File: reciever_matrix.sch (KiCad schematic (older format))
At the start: 1 part, among them J2 QUARTET_RECV

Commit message: Layout and route numpad matrix
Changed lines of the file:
@@
 $Descr A4 11693 8268
 encoding utf-8
-Sheet 3 3
+Sheet 3 4
 Title ""
 Date ""
@@
 AR Path="/5FF53271/5FF867A2" Ref="#PWR?"  Part="1"
 AR Path="/5FF53271/5FF7CBCC/5FF867A2" Ref="#PWR?"  Part="1"
-AR Path="/5FF5604D/5FF9299E/5FF867A2" Ref="#PWR?"  Part="1"
+AR Path="/5FF5604D/5FF9299E/5FF867A2" Ref="#PWR01"  Part="1"
 AR Path="/5FF77C9D/5FF867A2" Ref="#PWR03"  Part="1"
-F 0 "#PWR03" H 1350 950 50  0001 C CNN
+F 0 "#PWR01" H 1350 950 50  0001 C CNN
 F 1 "+5V" H 1365 1273 50  0000 C CNN
 F 2 "" H 1350 1100 50  0001 C CNN
@@
 AR Path="/5FF53271/5FF867A8" Ref="#PWR?"  Part="1"
 AR Path="/5FF53271/5FF7CBCC/5FF867A8" Ref="#PWR?"  Part="1"
-AR Path="/5FF5604D/5FF9299E/5FF867A8" Ref="#PWR?"  Part="1"
+AR Path="/5FF5604D/5FF9299E/5FF867A8" Ref="#PWR02"  Part="1"
 AR Path="/5FF77C9D/5FF867A8" Ref="#PWR04"  Part="1"
-F 0 "#PWR04" H 1350 1350 50  0001 C CNN
+F 0 "#PWR02" H 1350 1350 50  0001 C CNN
 F 1 "GND" H 1355 1427 50  0000 C CNN
 F 2 "" H 1350 1600 50  0001 C CNN
@@
 	1350 1400 1350 1500
 Connection ~ 1350 1500
-Text GLabel 1350 2250 0    50   Input ~ 0
-PD1
 Text GLabel 1350 2150 0    50   Input ~ 0
 PD0
-Text GLabel 1350 2350 0    50   Input ~ 0
-PD5
-Text GLabel 1350 2450 0    50   Input ~ 0
-PD6
-Text GLabel 1350 2550 0    50   Input ~ 0
-PD7
-Text GLabel 1350 2650 0    50   Input ~ 0
-PB0
-Text GLabel 1350 2750 0    50   Input ~ 0
-PB1
-Text GLabel 1350 2850 0    50   Input ~ 0
-PB2
-Text GLabel 1350 2950 0    50   Input ~ 0
-PC2
-Text GLabel 1350 3050 0    50   Input ~ 0
-PC3
 Text GLabel 1350 3150 0    50   Input ~ 0
 ADC7
-Wire Wire Line
-	1350 3150 1450 3150
-Wire Wire Line
-	1450 3050 1350 3050
-Wire Wire Line
-	1350 2950 1450 2950
-Wire Wire Line
-	1450 2850 1350 2850
-Wire Wire Line
-	1350 2750 1450 2750
-Wire Wire Line
-	1450 2650 1350 2650
-Wire Wire Line
-	1350 2550 1450 2550
-Wire Wire Line
-	1450 2450 1350 2450
-Wire Wire Line
-	1350 2350 1450 2350
-Wire Wire Line
-	1450 2250 1350 2250
-Wire Wire Line
-	1350 2150 1450 2150
 Text GLabel 1350 3350 0    50   Input ~ 0
 MISO
@@
 Text GLabel 1350 3550 0    50   Input ~ 0
 SCL
-Wire Wire Line
-	1350 3250 1450 3250
-Wire Wire Line
-	1350 3350 1450 3350
-Wire Wire Line
-	1350 3450 1450 3450
-Wire Wire Line
-	1350 3550 1450 3550
-Wire Wire Line
-	1350 3650 1450 3650
 $Comp
 L gigahawk:QUARTET_RECV J2
@@
 	1    0    0    -1
 $EndComp
+Text GLabel 1350 2250 0    50   Input ~ 0
+PD1
+Text GLabel 1350 2350 0    50   Input ~ 0
+PD5
+Text GLabel 1350 2450 0    50   Input ~ 0
+PD6
+Text GLabel 1350 2550 0    50   Input ~ 0
+PD7
+Text GLabel 1350 2650 0    50   Input ~ 0
+PB0
+Text GLabel 1350 2750 0    50   Input ~ 0
+PB1
+Text GLabel 1350 2850 0    50   Input ~ 0
+PB2
+Text GLabel 1350 2950 0    50   Input ~ 0
+PC2
+Text GLabel 1350 3050 0    50   Input ~ 0
+PC3
+Wire Wire Line
+	1450 2150 1350 2150
+Wire Wire Line
+	1350 2250 1450 2250
+Wire Wire Line
+	1450 2350 1350 2350
+Wire Wire Line
+	1350 2450 1450 2450
+Wire Wire Line
+	1450 2550 1350 2550
+Wire Wire Line
+	1350 2650 1450 2650
+Wire Wire Line
+	1450 2750 1350 2750
+Wire Wire Line
+	1350 2850 1450 2850
+Wire Wire Line
+	1450 2950 1350 2950
+Wire Wire Line
+	1350 3050 1450 3050
+Wire Wire Line
+	1450 3150 1350 3150
+Wire Wire Line
+	1350 3250 1450 3250
+Wire Wire Line
+	1350 3350 1450 3350
+Wire Wire Line
+	1450 3450 1350 3450
+Wire Wire Line
+	1350 3550 1450 3550
+Wire Wire Line
+	1450 3650 1350 3650
 $EndSCHEMATC

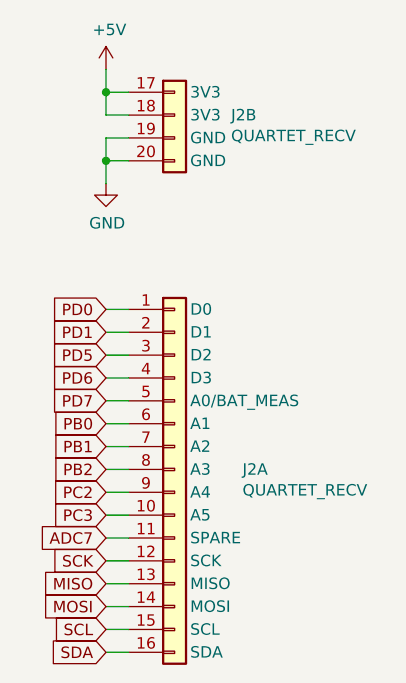
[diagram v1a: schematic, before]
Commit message: Reroute matrix, redo schematics for feather compat
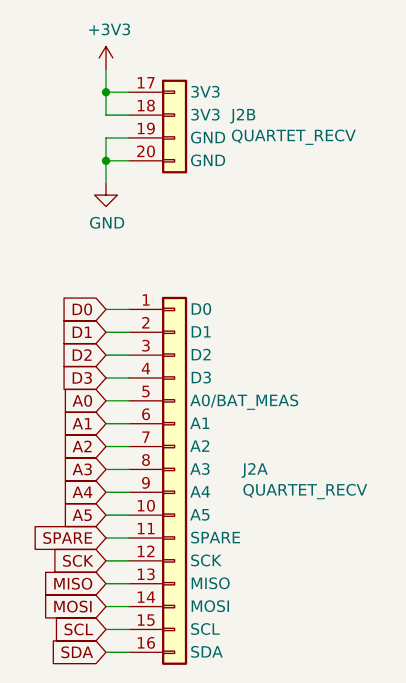
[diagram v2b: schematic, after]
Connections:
- net +5V renamed +3V3
- net ADC7 renamed SPARE
- net PB0 renamed A1
- net PB1 renamed A2
- net PB2 renamed A3
- net PC2 renamed A4
- net PC3 renamed A5
- net PD0 renamed D0
- net PD1 renamed D1
- net PD5 renamed D2
- net PD6 renamed D3
- net PD7 renamed A0
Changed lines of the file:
@@
 $EndDescr
-$Comp
-L power:+5V #PWR?
-U 1 1 5FF867A2
-P 1350 1100
-AR Path="/5FF53271/5FF867A2" Ref="#PWR?"  Part="1"
-AR Path="/5FF53271/5FF7CBCC/5FF867A2" Ref="#PWR?"  Part="1"
-AR Path="/5FF5604D/5FF9299E/5FF867A2" Ref="#PWR01"  Part="1"
-AR Path="/5FF77C9D/5FF867A2" Ref="#PWR03"  Part="1"
-F 0 "#PWR01" H 1350 950 50  0001 C CNN
-F 1 "+5V" H 1365 1273 50  0000 C CNN
-F 2 "" H 1350 1100 50  0001 C CNN
-F 3 "" H 1350 1100 50  0001 C CNN
-	1    1350 1100
-	1    0    0    -1
-$EndComp
 $Comp
 L power:GND #PWR?
@@
 Connection ~ 1350 1500
 Text GLabel 1350 2150 0    50   Input ~ 0
-PD0
+D0
 Text GLabel 1350 3150 0    50   Input ~ 0
-ADC7
+SPARE
 Text GLabel 1350 3350 0    50   Input ~ 0
 MISO
@@
 U 1 1 5FF8174A
 P 1650 2100
+AR Path="/5FF8174A" Ref="J2"  Part="1"
+AR Path="/5FF77C9D/5FF8174A" Ref="J2"  Part="1"
+AR Path="/5FF5604D/5FF9299E/5FF8174A" Ref="J2"  Part="1"
 F 0 "J2" H 1947 1350 50  0000 L CNN
 F 1 "QUARTET_RECV" H 1947 1259 50  0000 L CNN
@@
 U 2 1 5FF82748
 P 1650 1150
+AR Path="/5FF82748" Ref="J2"  Part="2"
+AR Path="/5FF77C9D/5FF82748" Ref="J2"  Part="2"
+AR Path="/5FF5604D/5FF9299E/5FF82748" Ref="J2"  Part="2"
 F 0 "J2" H 1897 1000 50  0000 L CNN
 F 1 "QUARTET_RECV" H 1897 909 50  0000 L CNN
@@
 $EndComp
 Text GLabel 1350 2250 0    50   Input ~ 0
-PD1
+D1
 Text GLabel 1350 2350 0    50   Input ~ 0
-PD5
+D2
 Text GLabel 1350 2450 0    50   Input ~ 0
-PD6
+D3
 Text GLabel 1350 2550 0    50   Input ~ 0
-PD7
+A0
 Text GLabel 1350 2650 0    50   Input ~ 0
-PB0
+A1
 Text GLabel 1350 2750 0    50   Input ~ 0
-PB1
+A2
 Text GLabel 1350 2850 0    50   Input ~ 0
-PB2
+A3
 Text GLabel 1350 2950 0    50   Input ~ 0
-PC2
+A4
 Text GLabel 1350 3050 0    50   Input ~ 0
-PC3
+A5
 Wire Wire Line
 	1450 2150 1350 2150
@@
 Wire Wire Line
 	1450 3650 1350 3650
+$Comp
+L power:+3V3 #PWR0110
+U 1 1 60477128
+P 1350 1100
+F 0 "#PWR0110" H 1350 950 50  0001 C CNN
+F 1 "+3V3" H 1365 1273 50  0000 C CNN
+F 2 "" H 1350 1100 50  0001 C CNN
+F 3 "" H 1350 1100 50  0001 C CNN
+	1    1350 1100
+	1    0    0    -1
+$EndComp
 $EndSCHEMATC

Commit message: Get ready for JLCPCB
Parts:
- J2: Part Numbers (none) -> F519-1A7A1-11004-E200; F519-1A7A1-11016-E200
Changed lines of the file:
@@
 $Descr A4 11693 8268
 encoding utf-8
-Sheet 3 4
+Sheet 3 3
 Title ""
 Date ""
@@
 AR Path="/5FF5604D/5FF9299E/5FF867A8" Ref="#PWR02"  Part="1"
 AR Path="/5FF77C9D/5FF867A8" Ref="#PWR04"  Part="1"
-F 0 "#PWR02" H 1350 1350 50  0001 C CNN
+F 0 "#PWR04" H 1350 1350 50  0001 C CNN
 F 1 "GND" H 1355 1427 50  0000 C CNN
 F 2 "" H 1350 1600 50  0001 C CNN
@@
 F 2 "Gigahawk:QUARTET_RECV_MATRIX" H 1700 2100 50  0001 C CNN
 F 3 "" H 1700 2100 50  0001 C CNN
+F 4 "F519-1A7A1-11004-E200; F519-1A7A1-11016-E200" H 1650 2100 50  0001 C CNN "Part Numbers"
 	1    1650 2100
 	1    0    0    -1
